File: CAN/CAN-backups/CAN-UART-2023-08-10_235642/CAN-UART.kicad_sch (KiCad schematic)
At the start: 24 parts, among them CN1 1.0T-4PLTPZ, J1 Conn_01x04, J2 Screw_Terminal_01x02, P1 USB_C_Plug_USB2.0, Q1 BSS214NW, Q2 BSS214NW, U1 AP2112K-3.3, U2 SN65HVD230, U5 ESP32-C3-MINI-1

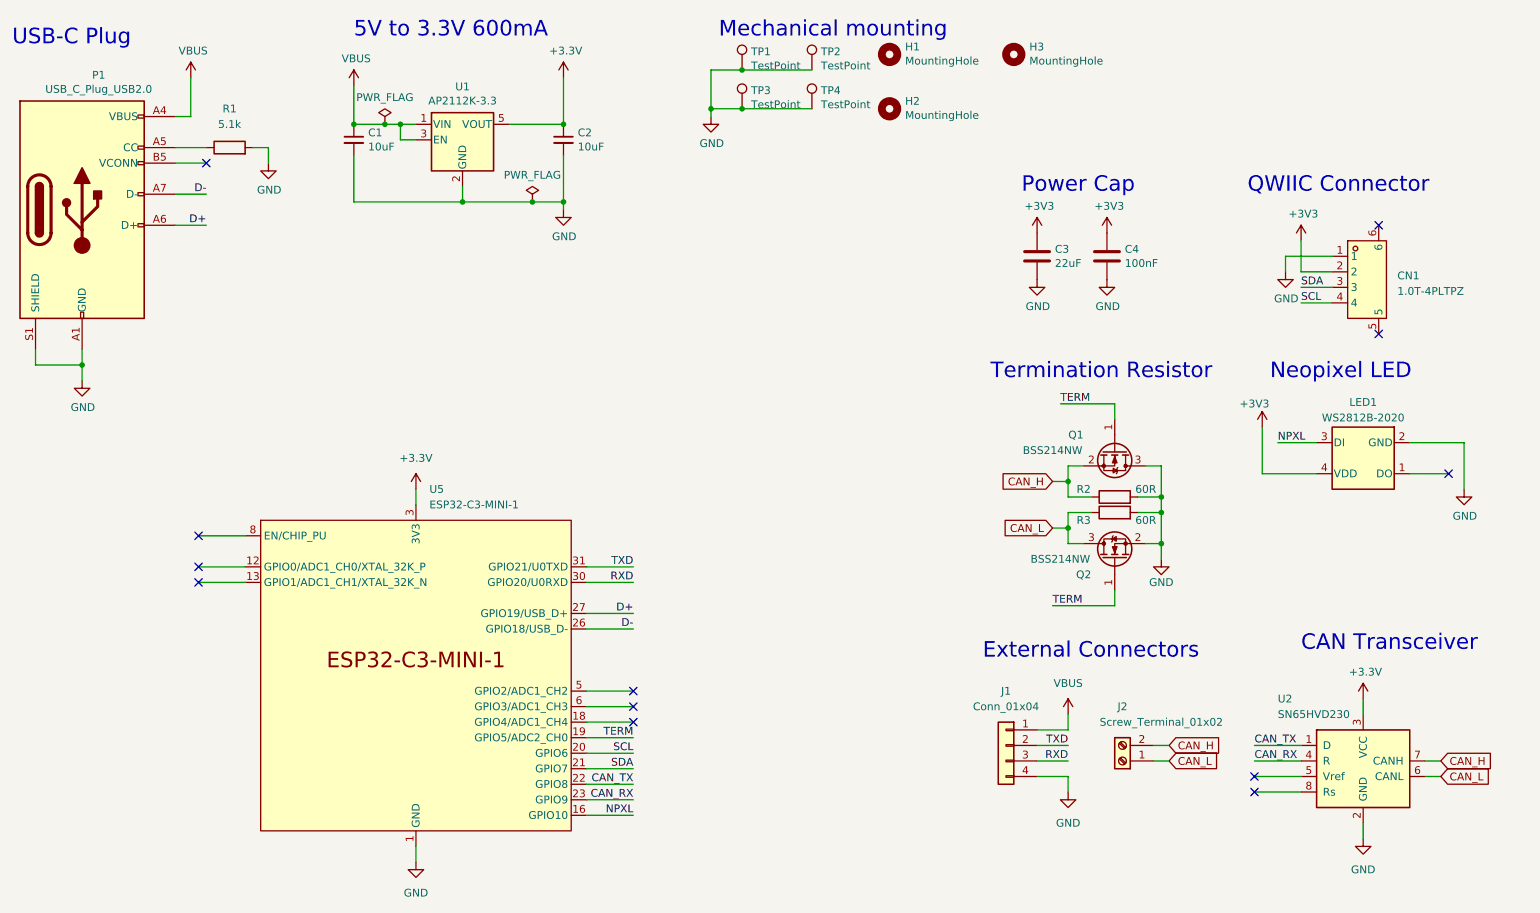
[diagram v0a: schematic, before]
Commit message: Removed PD
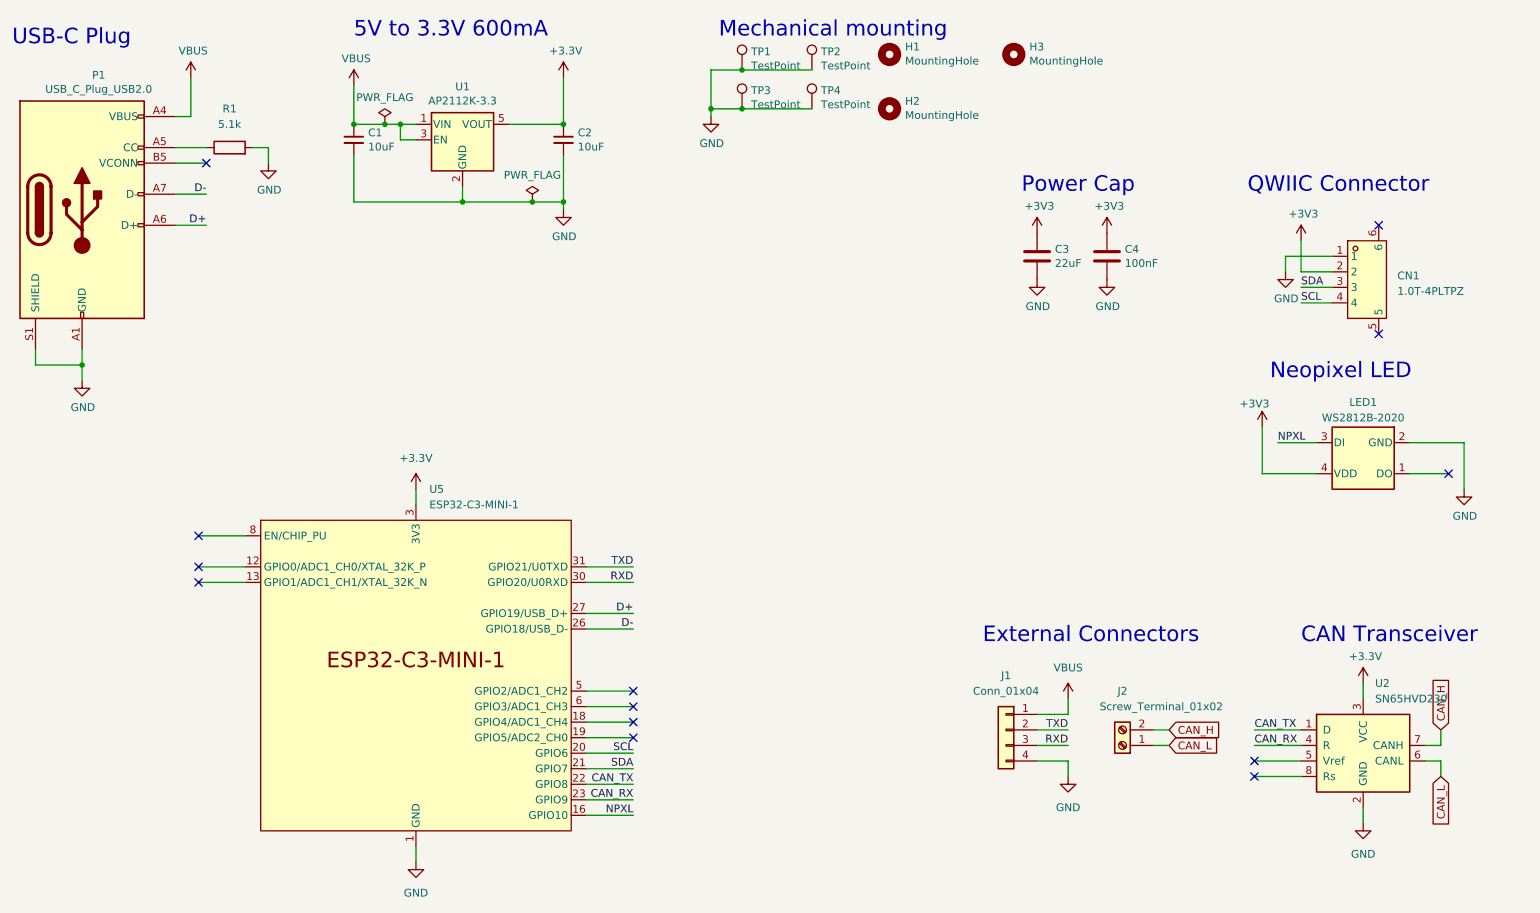
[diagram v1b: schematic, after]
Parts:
- removed Q1, Q2: BSS214NW, Package_TO_SOT_SMD:SOT-323_SC-70, symbol Transistor_FET:BSS214NW
- removed R2, R3: 60R, Resistor_SMD:R_0402_1005Metric_Pad0.72x0.64mm_HandSolder, symbol Device:R
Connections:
- net TERM: no longer names the net of U5.19 (GPIO5/ADC2_CH0)
- no-connect marks 12 -> 13
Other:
- note removed: "Termination Resistor"
- moved on the sheet: J1, J2, U2
